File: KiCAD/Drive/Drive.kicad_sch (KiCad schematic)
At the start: 57 parts, among them U1 L7812, U2 LM324

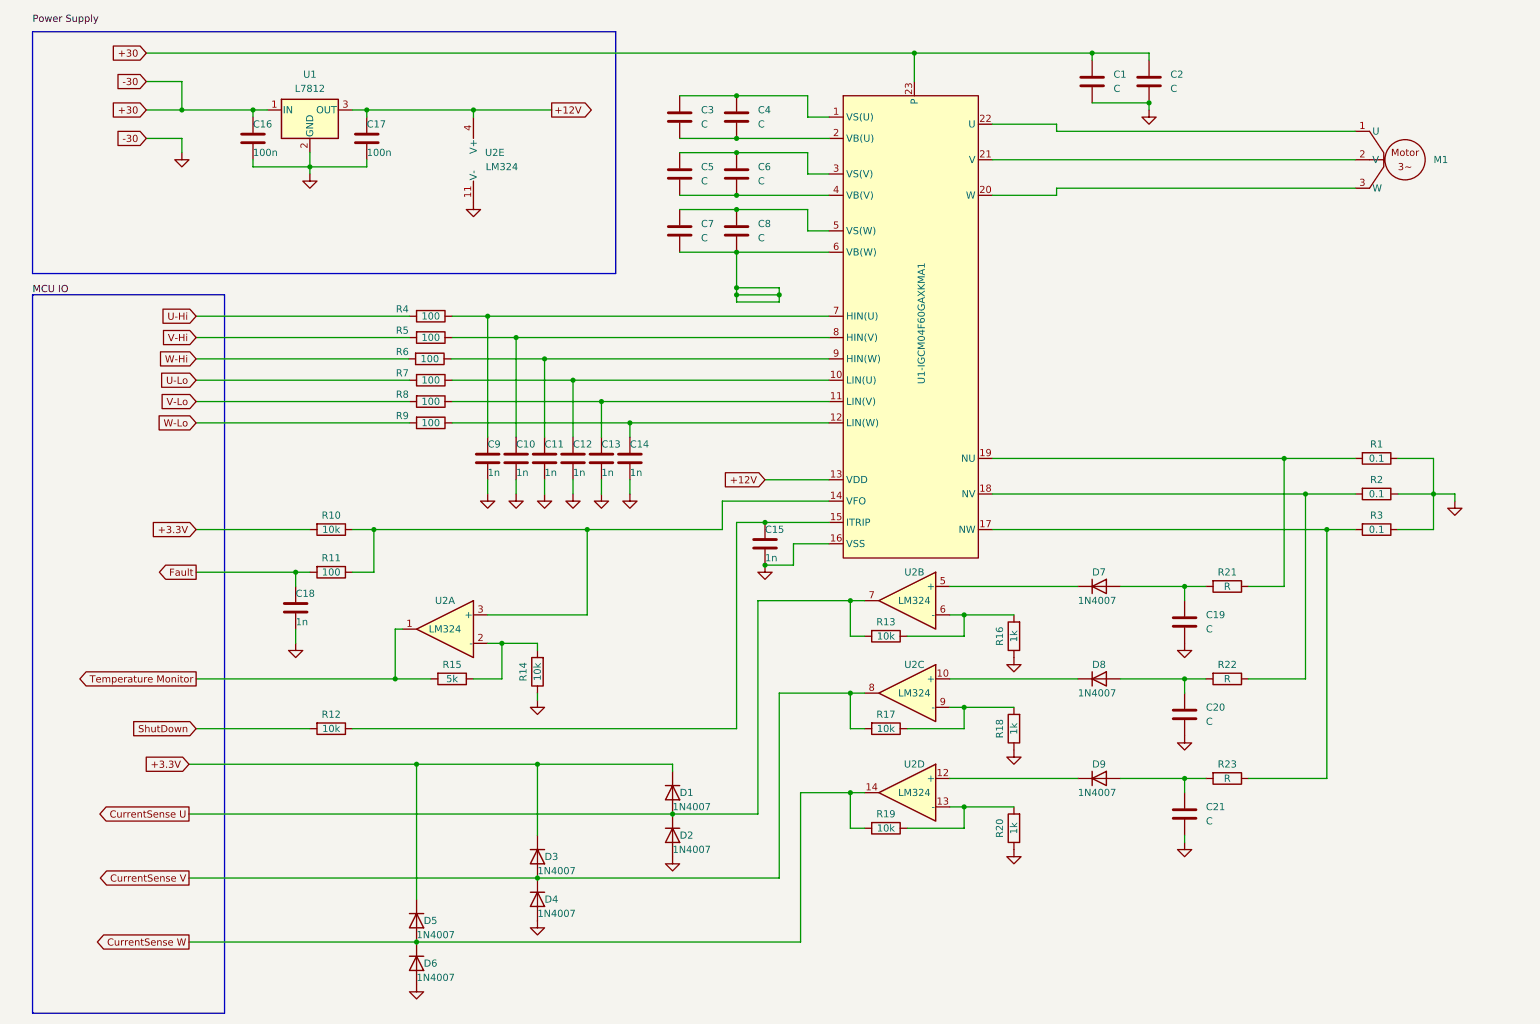
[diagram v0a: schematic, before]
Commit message: adds code for motor to run
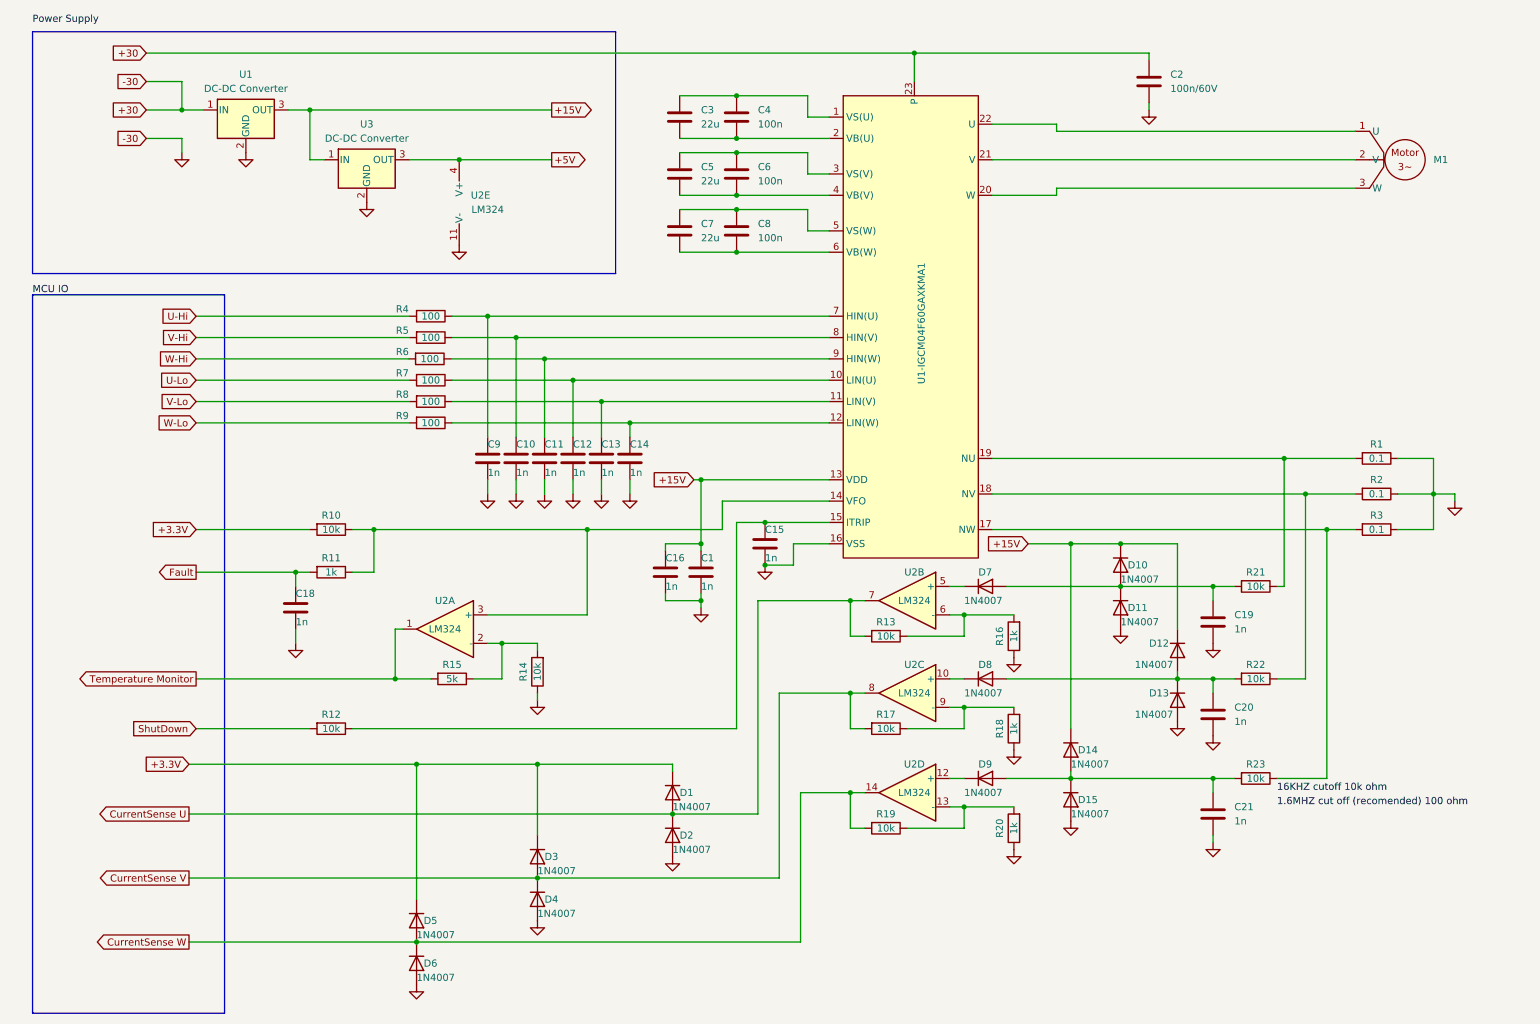
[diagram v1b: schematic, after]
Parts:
- removed C17: 100n, symbol Device:C
- added D10, D11, D12, D13, D14, D15: 1N4007, symbol Device:D
- added U3: DC-DC Converter, symbol Regulator_Linear:L7812
- C1, C19, C20, C21: value C -> 1n
- C16: value 100n -> 1n
- C2: value C -> 100n/60V
- C3, C5, C7: value C -> 22u
- C4, C6, C8: value C -> 100n
- R11: value 100 -> 1k
- R21, R22, R23: value R -> 10k
- U1: value L7812 -> DC-DC Converter
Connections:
- net GND: now also D11.2 (A), D13.2 (A), D15.2 (A), U3.2 (GND); no longer C1.1, C16.1
- net at C21.1, D9.2 (A), R23.2: now also D14.2 (A), D15.1 (K)
- net at C20.1, D8.2 (A), R22.2: now also D12.2 (A), D13.1 (K)
- net at C19.1, D7.2 (A), R21.2: now also D10.2 (A), D11.1 (K)
- net +12V renamed +15V
- net +15V: now also C1.1, C16.1, D10.1 (K), D12.1 (K), D14.1 (K), U3.1 (IN); no longer U2.4 (V+)
- new net +5V: U2.4 (V+), U3.3 (OUT)
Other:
- moved on the sheet: C19, C20, C21, D7, D8, D9, R21, R22, R23, U1, U2E

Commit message: adds circuit diagram and pcb
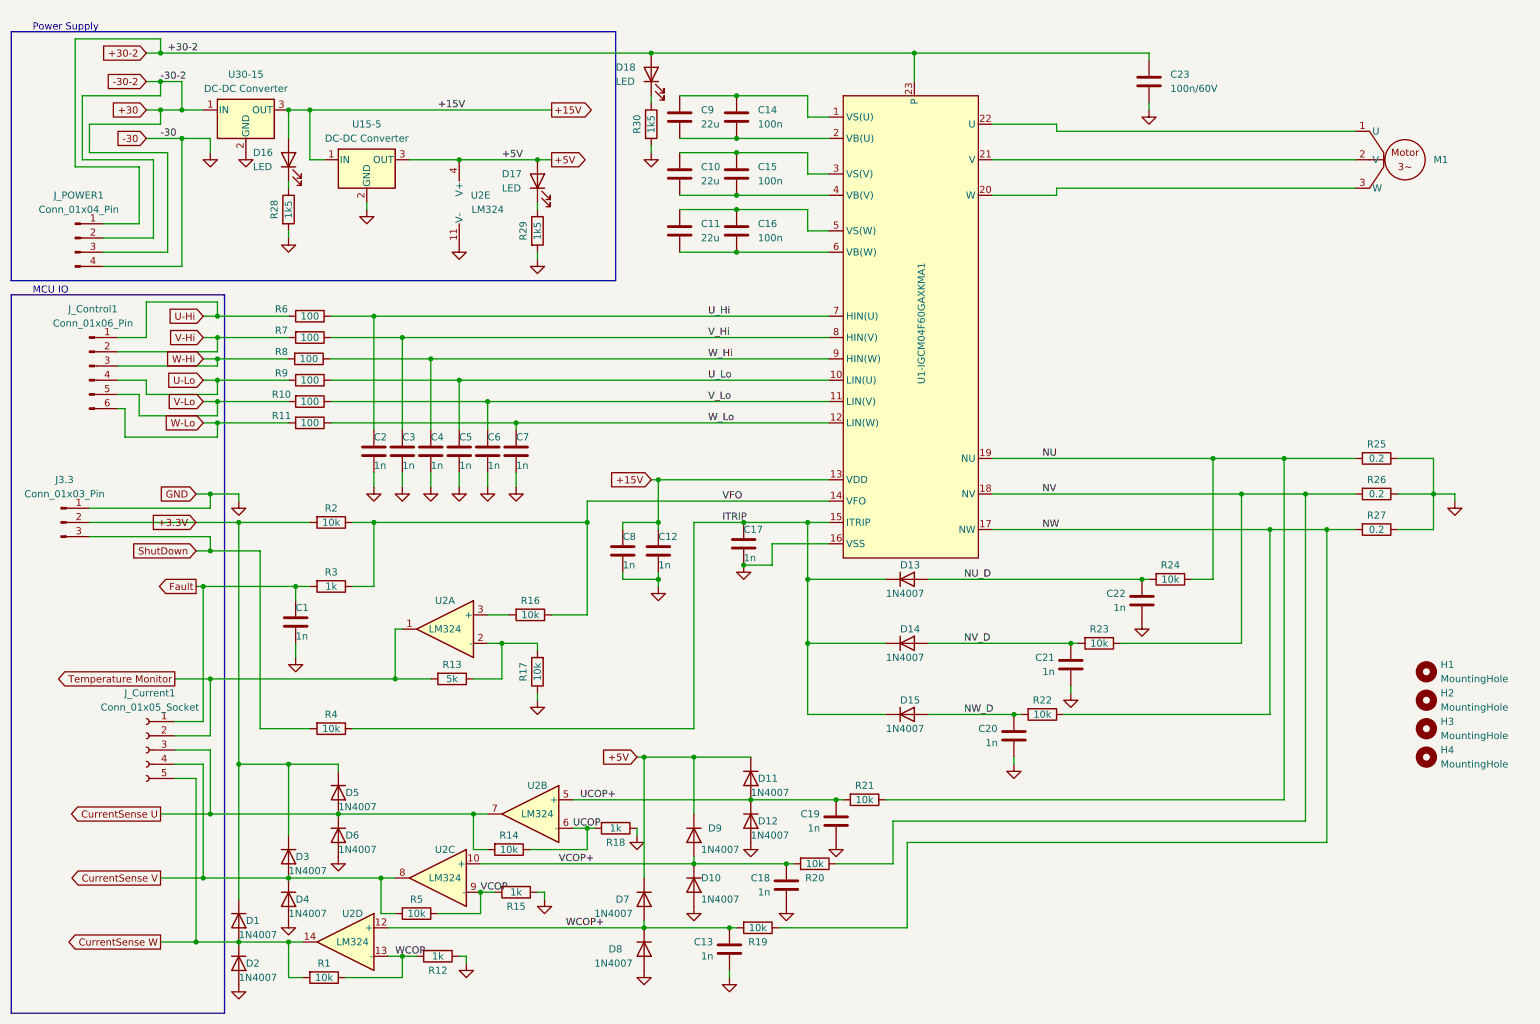
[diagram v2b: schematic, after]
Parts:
- removed D7, D8, D9: 1N4007, symbol Device:D
- removed R18, R20: 1k, symbol Device:R
- added C20, C21, C22: 1n, Capacitor_SMD:C_1206_3216Metric, symbol Device:C
- added D13, D14, D15: 1N4007, Diode_SMD:D_SOD-323, symbol Device:D
- added D16, D17, D18: LED, LED_SMD:LED_1206_3216Metric, symbol Device:LED
- added H1, H2, H3, H4: MountingHole, MountingHole:MountingHole_3.5mm, symbol Mechanical:MountingHole
- added J3.3: Conn_01x03_Pin, Connector_PinHeader_2.54mm:PinHeader_1x03_P2.54mm_Vertical, symbol Connector:Conn_01x03_Pin
- added J_Control1: Conn_01x06_Pin, Connector_PinHeader_2.54mm:PinHeader_1x06_P2.54mm_Vertical, symbol Connector:Conn_01x06_Pin
- added J_Current1: Conn_01x05_Socket, Connector_PinHeader_2.54mm:PinHeader_1x05_P2.54mm_Vertical, symbol Connector:Conn_01x05_Socket
- added J_POWER1: Conn_01x04_Pin, Connector_PinHeader_2.54mm:PinHeader_1x04_P2.54mm_Vertical, symbol Connector:Conn_01x04_Pin
- added R12, R15: 1k, Resistor_SMD:R_1206_3216Metric, symbol Device:R
- added R16, R22, R23, R24: 10k, Resistor_SMD:R_1206_3216Metric, symbol Device:R
- added R28, R29, R30: 1k5, Resistor_SMD:R_1206_3216Metric, symbol Device:R
- C1: renamed from C18; footprint (none) -> Capacitor_SMD:C_1206_3216Metric
- C10: renamed from C5; footprint (none) -> Capacitor_THT:C_Radial_D4.0mm_H7.0mm_P1.50mm
- C11: renamed from C7; footprint (none) -> Capacitor_THT:C_Radial_D4.0mm_H7.0mm_P1.50mm
- C12: renamed from C1; footprint (none) -> Capacitor_SMD:C_1206_3216Metric
- C13: renamed from C21; footprint (none) -> Capacitor_SMD:C_1206_3216Metric
- C14: renamed from C4; footprint (none) -> Capacitor_SMD:C_1206_3216Metric
- C15: renamed from C6; footprint (none) -> Capacitor_SMD:C_1206_3216Metric
- C16: renamed from C8; footprint (none) -> Capacitor_SMD:C_1206_3216Metric
- C17: renamed from C15; footprint (none) -> Capacitor_SMD:C_1206_3216Metric
- C18: renamed from C20; footprint (none) -> Capacitor_SMD:C_1206_3216Metric
- C19: footprint (none) -> Capacitor_SMD:C_1206_3216Metric
- C2: renamed from C9; footprint (none) -> Capacitor_SMD:C_1206_3216Metric
- C23: renamed from C2; footprint (none) -> Capacitor_SMD:C_1206_3216Metric
- C3: renamed from C10; footprint (none) -> Capacitor_SMD:C_1206_3216Metric
- C4: renamed from C11; footprint (none) -> Capacitor_SMD:C_1206_3216Metric
- C5: renamed from C12; footprint (none) -> Capacitor_SMD:C_1206_3216Metric
- C6: renamed from C13; footprint (none) -> Capacitor_SMD:C_1206_3216Metric
- C7: renamed from C14; footprint (none) -> Capacitor_SMD:C_1206_3216Metric
- C8: renamed from C16; footprint (none) -> Capacitor_SMD:C_1206_3216Metric
- C9: renamed from C3; footprint (none) -> Capacitor_THT:C_Radial_D4.0mm_H7.0mm_P1.50mm
- D1: renamed from D5; footprint (none) -> Diode_SMD:D_SOD-323
- D10: renamed from D13; footprint (none) -> Diode_SMD:D_SOD-323
- D11: renamed from D10; footprint (none) -> Diode_SMD:D_SOD-323
- D12: renamed from D11; footprint (none) -> Diode_SMD:D_SOD-323
- D2: renamed from D6; footprint (none) -> Diode_SMD:D_SOD-323
- D3, D4: footprint (none) -> Diode_SMD:D_SOD-323
- D5: renamed from D1; footprint (none) -> Diode_SMD:D_SOD-323
- D6: renamed from D2; footprint (none) -> Diode_SMD:D_SOD-323
- D7: renamed from D14; footprint (none) -> Diode_SMD:D_SOD-323
- D8: renamed from D15; footprint (none) -> Diode_SMD:D_SOD-323
- D9: renamed from D12; footprint (none) -> Diode_SMD:D_SOD-323
- M1: footprint (none) -> Connector_PinHeader_2.54mm:PinHeader_1x03_P2.54mm_Vertical
- R1: renamed from R19; footprint (none) -> Resistor_SMD:R_1206_3216Metric
- R10: renamed from R8; footprint (none) -> Resistor_SMD:R_1206_3216Metric
- R11: renamed from R9; footprint (none) -> Resistor_SMD:R_1206_3216Metric
- R13: renamed from R15; footprint (none) -> Resistor_SMD:R_1206_3216Metric
- R14: renamed from R13; footprint (none) -> Resistor_SMD:R_1206_3216Metric
- R17: renamed from R14; footprint (none) -> Resistor_SMD:R_1206_3216Metric
- R18: renamed from R16; footprint (none) -> Resistor_SMD:R_1206_3216Metric
- R19: renamed from R23; footprint (none) -> Resistor_SMD:R_1206_3216Metric
- R2: renamed from R10; footprint (none) -> Resistor_SMD:R_1206_3216Metric
- R20: renamed from R22; footprint (none) -> Resistor_SMD:R_1206_3216Metric
- R21: footprint (none) -> Resistor_SMD:R_1206_3216Metric
- R25: renamed from R1; value 0.1 -> 0.2; footprint (none) -> Resistor_THT:R_Axial_DIN0204_L3.6mm_D1.6mm_P1.90mm_Vertical
- R26: renamed from R2; value 0.1 -> 0.2; footprint (none) -> Resistor_THT:R_Axial_DIN0204_L3.6mm_D1.6mm_P1.90mm_Vertical
- R27: renamed from R3; value 0.1 -> 0.2; footprint (none) -> Resistor_THT:R_Axial_DIN0204_L3.6mm_D1.6mm_P1.90mm_Vertical
- R3: renamed from R11; footprint (none) -> Resistor_SMD:R_1206_3216Metric
- R4: renamed from R12; footprint (none) -> Resistor_SMD:R_1206_3216Metric
- R5: renamed from R17; footprint (none) -> Resistor_SMD:R_1206_3216Metric
- R6: renamed from R4; footprint (none) -> Resistor_SMD:R_1206_3216Metric
- R7: renamed from R5; footprint (none) -> Resistor_SMD:R_1206_3216Metric
- R8: renamed from R6; footprint (none) -> Resistor_SMD:R_1206_3216Metric
- R9: renamed from R7; footprint (none) -> Resistor_SMD:R_1206_3216Metric
- U1-IGCM04F60GAXKMA1: footprint (none) -> Bridge:IGCM04F60GAXKMA1
- U15-5: renamed from U3; footprint (none) -> Connector_PinHeader_2.54mm:PinHeader_1x03_P2.54mm_Vertical
- U2: footprint (none) -> Package_SO:SSOP-14_5.3x6.2mm_P0.65mm
- U30-15: renamed from U1; footprint (none) -> Connector_PinHeader_2.54mm:PinHeader_1x03_P2.54mm_Vertical
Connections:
- net +15V: now also D16.2 (A); no longer D11.1 (K), D7.1 (K), D9.1 (K)
- net +3.3V: now also J3.3.2 (Pin_2)
- net +5V: now also D11.1 (K), D7.1 (K), D9.1 (K), D17.2 (A)
- net CurrentSense U: now also J_Current1.3 (Pin_3)
- net CurrentSense V: now also J_Current1.4 (Pin_4)
- net CurrentSense W: now also J_Current1.5 (Pin_5)
- net Fault: now also J_Current1.1 (Pin_1)
- net GND: now also C20.2, C21.2, C22.2, J3.3.1 (Pin_1), J_POWER1.4 (Pin_4), R12.1, R15.1, R28.2, R29.2, R30.2; no longer C23.1, U1-IGCM04F60GAXKMA1.23 (P), U30-15.1 (IN)
- net ShutDown: now also J3.3.3 (Pin_3)
- net Temperature Monitor: now also J_Current1.2 (Pin_2)
- net U-Hi: now also J_Control1.1 (Pin_1)
- net U-Lo: now also J_Control1.4 (Pin_4)
- net V-Hi: now also J_Control1.2 (Pin_2)
- net V-Lo: now also J_Control1.5 (Pin_5)
- net W-Hi: now also J_Control1.3 (Pin_3)
- net W-Lo: now also J_Control1.6 (Pin_6)
- net VFO: now reaches R2.1, R3.1, U1-IGCM04F60GAXKMA1.14 (VFO)
- net VFO: now also R16.1; no longer U2.3 (+)
- net WCOP+: now reaches U2.12 (+)
- net WCOP+: now also C13.1, D7.2 (A), D8.1 (K), R19.2
- net WCOP-: now reaches R1.1, U2.13 (-)
- net WCOP-: now also R12.2
- net V_Lo: now reaches C6.1, R10.1, U1-IGCM04F60GAXKMA1.11 (LIN(V))
- net UCOP-: now reaches R14.1, R18.2, U2.6 (-)
- net NU: now reaches R21.1, R25.2, U1-IGCM04F60GAXKMA1.19 (NU)
- net NU: now also R24.1
- net U_Lo: now reaches C5.1, R9.1, U1-IGCM04F60GAXKMA1.10 (LIN(U))
- net U_Hi: now reaches C2.1, R6.1, U1-IGCM04F60GAXKMA1.7 (HIN(U))
- net NV: now reaches R20.1, R26.2, U1-IGCM04F60GAXKMA1.18 (NV)
- net NV: now also R23.1
- net W_Lo: now reaches C7.1, R11.1, U1-IGCM04F60GAXKMA1.12 (LIN(W))
- net W_Hi: now reaches C4.1, R8.1, U1-IGCM04F60GAXKMA1.9 (HIN(W))
- net NW: now reaches R19.1, R27.2, U1-IGCM04F60GAXKMA1.17 (NW)
- net NW: now also R22.1
- net VCOP+: now reaches C18.1, D10.1 (K), D9.2 (A), R20.2
- net VCOP+: now also U2.10 (+)
- net V_Hi: now reaches C3.1, R7.1, U1-IGCM04F60GAXKMA1.8 (HIN(V))
- net UCOP+: now reaches U2.5 (+)
- net UCOP+: now also C19.1, D11.2 (A), D12.1 (K), R21.2
- net VCOP-: now reaches R5.1, U2.9 (-)
- net VCOP-: now also R15.2
- net ITRIP: now reaches C17.1, R4.1, U1-IGCM04F60GAXKMA1.15 (ITRIP)
- net ITRIP: now also D13.1 (K), D14.1 (K), D15.1 (K)
- new net: R16.2, U2.3 (+)
- new net: D18.1 (K), R30.1
- new net: D17.1 (K), R29.1
- new net: D16.1 (K), R28.1
- new net +30: J_POWER1.2 (Pin_2), J_POWER1.3 (Pin_3), U30-15.1 (IN)
- new net +30-2: C23.1, D18.2 (A), J_POWER1.1 (Pin_1), U1-IGCM04F60GAXKMA1.23 (P)
- new net NU_D: C22.1, D13.2 (A), R24.2
- new net NV_D: C21.1, D14.2 (A), R23.2
- new net NW_D: C20.1, D15.2 (A), R22.2
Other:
- note added: "MCU IO"
- note added: "Power Supply"
- moved on the sheet: C1, C12, C13, C17, C18, C19, C2, C3, C4, C5, C6, C7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

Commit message: testing with PCB
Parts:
- R28: value 1k5 -> 5k
- R30: value 1k5 -> 10k
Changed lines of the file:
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@@
       (effects (font (size 1.27 1.27)))
     )
-    (property "Value" "1k5" (at 64.77 49.53 90)
+    (property "Value" "5k" (at 64.77 49.53 90)
       (effects (font (size 1.27 1.27)))
     )
@@
       (effects (font (size 1.27 1.27)))
     )
-    (property "Value" "1k5" (at 129.54 34.29 90)
-      (effects (font (size 1.27 1.27)))
-    )
+    (property "Value" "10k" (at 129.54 34.29 90)
+      (effects (font (size 1.27 1.27)))
+    )
